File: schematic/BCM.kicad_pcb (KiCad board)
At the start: 4 copper layers, 67 parts, among them P401 POWERCON, P402 KEYSWITCH, P403 CHARGESW, P601 BRUSA_CANCON, P602 A123_CANCON, P603 CON+, P604 CON-, P605 CONPRE, P606 UART, Q1 IRF7101PbF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

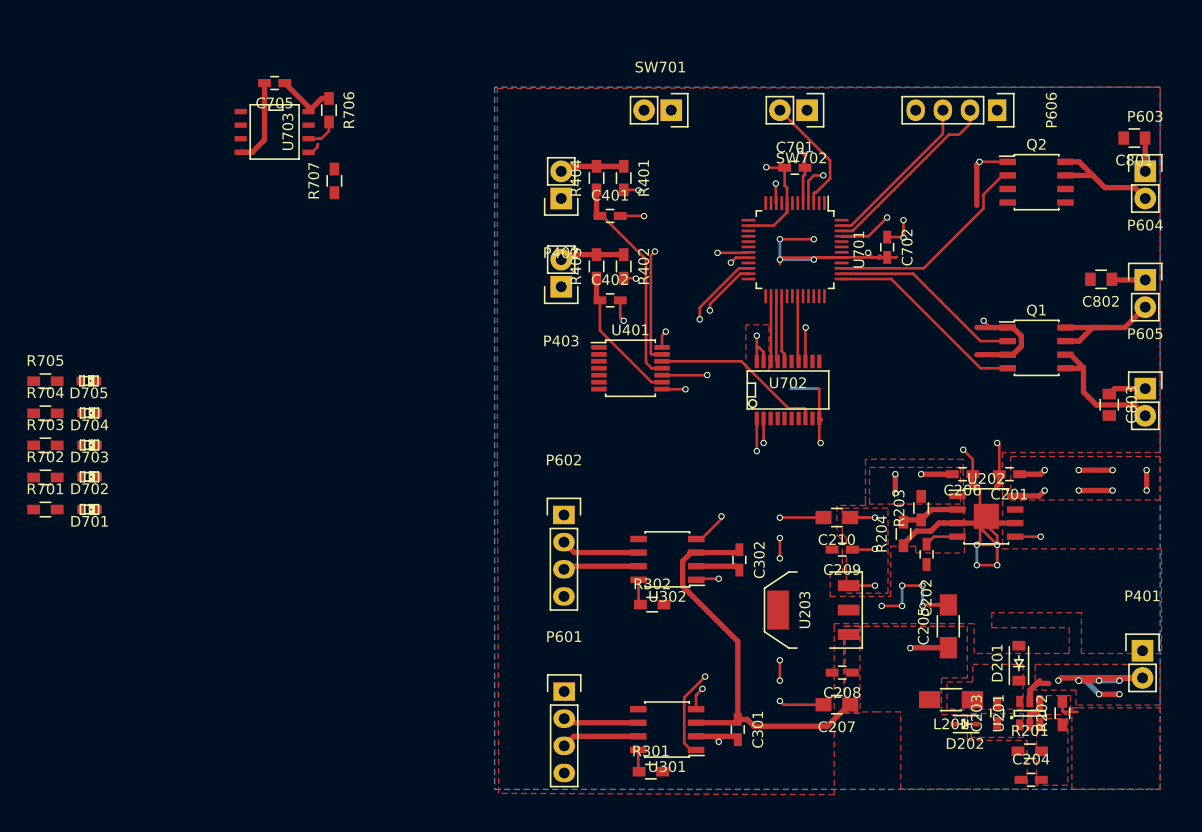
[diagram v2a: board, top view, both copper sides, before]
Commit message: [routing] finished routing passed all DRCs moved pins to accomodate routing
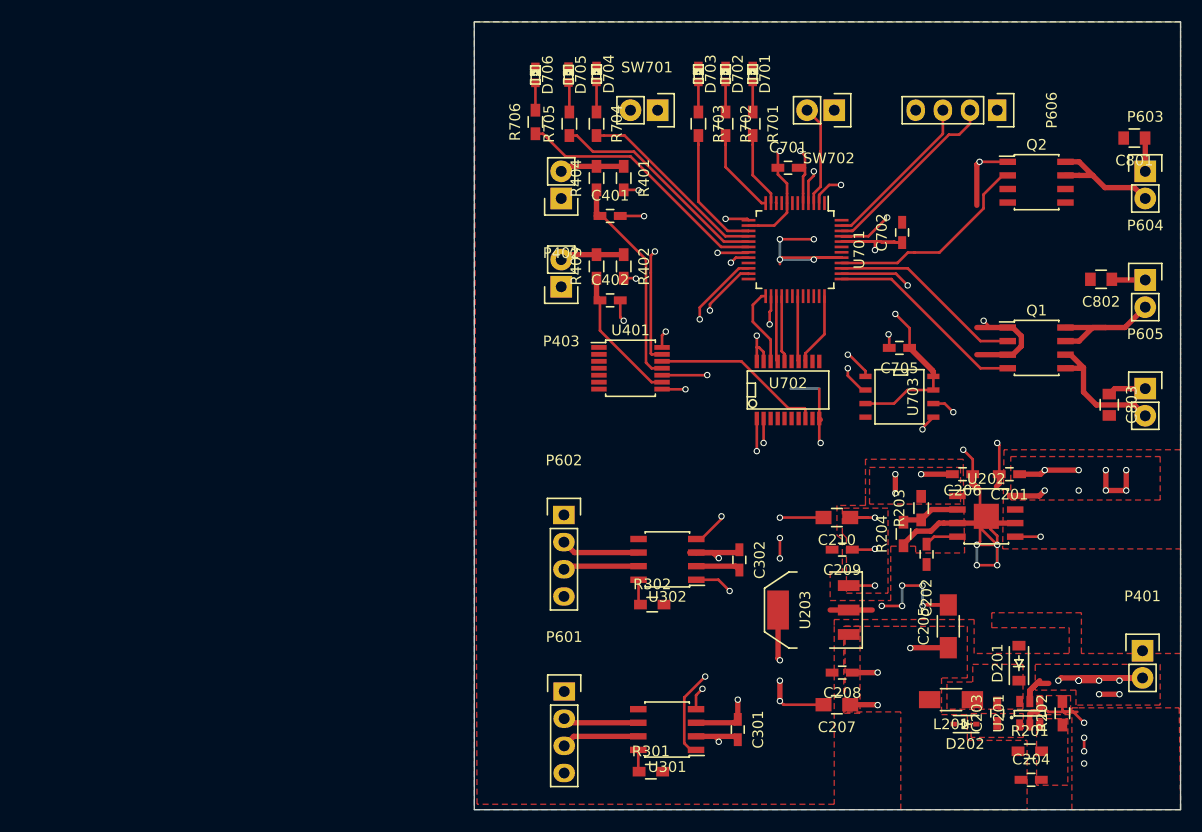
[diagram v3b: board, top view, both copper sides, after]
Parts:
- removed R707: 1k, Resistors_SMD:R_0603_HandSoldering
- added D706: RED, LEDs:LED-0603, F.Cu at (114.3, 121.2)
- R701, R702, R703, R704, R705: value 330 -> 1k
- U703: value 24C16 -> AT25XX
- moved R701 75.3 mm to (134.6, 125.7), turned to 270 degrees
- moved D701 74.2 mm to (134.6, 121.1), turned to 270 degrees
- moved R702 71.7 mm to (132.1, 125.7), turned to 270 degrees
- moved D702 70.4 mm to (132.1, 121.1), turned to 270 degrees
- moved R703 68.1 mm to (129.5, 125.7), turned to 270 degrees
- moved D703 66.7 mm to (129.5, 121.1), turned to 270 degrees
- moved C705 63.5 mm to (148.3, 146.7)
- moved U703 63.5 mm to (148.3, 151.3)
- moved R704 58.2 mm to (120.0, 125.7), turned to 270 degrees
- moved D704 57.0 mm to (120.0, 121.1), turned to 270 degrees
- moved R705 54.6 mm to (117.5, 125.7), turned to 90 degrees
- moved D705 53.2 mm to (117.4, 121.1), turned to 270 degrees
- moved R706 19.3 mm to (114.3, 125.6), turned to 90 degrees
- moved SW702 2.54 mm to (142.2, 124.5)
- moved C702 1.97 mm to (148.6, 135.9), turned to 90 degrees
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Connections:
- C209 pad 1: VCC -> +3V3
- C210 pad 1: VCC -> +3V3
- C701 pad 1: VCC -> +3V3
- C702 pad 1: VCC -> +3V3
- C705 pad 1: VCC -> +3V3
- R401 pad 2: VCC -> +3V3
- R402 pad 2: VCC -> +3V3
- R701 pad 2: /microController/IO_LED03 -> /microController/IO_LED0
- R702 pad 2: /microController/IO_LED02 -> /microController/IO_LED1
- R703 pad 2: Net-(R703-Pad2) -> /microController/IO_LED2
- R704 pad 2: /microController/IO_LED00 -> /microController/IO_LED3
- R705 pad 1: /microController/IO_LED10 -> /microController/IO_LED4
- R706 pad 1: VCC -> /microController/IO_LED5
- R706 pad 2: /microController/EEPROM_SCL -> Net-(D706-Pad2)
- U203 pad 3: VCC -> +3V3
- U401 pad 14: VCC -> +3V3
- U701 pad 10: /microController/CAN1_INT -> Net-(U701-Pad10)
- U701 pad 11: Net-(U701-Pad11) -> /microController/IO_LED0
- U701 pad 12: Net-(U701-Pad12) -> /microController/IO_LED1
- U701 pad 13: Net-(U701-Pad13) -> /microController/PROM_SCK
- U701 pad 14: VCC -> +3V3
- U701 pad 15: /microController/EEPROM_SCL -> /microController/IO_LED2
- U701 pad 16: /microController/EEPROM_SDA -> /microController/IO_LED3
- U701 pad 17: Net-(U701-Pad17) -> /microController/IO_LED4
- U701 pad 18: Net-(U701-Pad18) -> /microController/IO_LED5
- U701 pad 2: Net-(U701-Pad2) -> /microController/PROM_SSEL
- U701 pad 25: /microController/IO_LED10 -> /microController/CAN1_SSEL
- U701 pad 26: /microController/CAN1_SSEL -> /microController/PROM_MISO
- U701 pad 36: /microController/IO_LED00 -> /microController/CAN1_INT
- U701 pad 38: /Contactor Driver/CON- -> /microController/PROM_MOSI
- U701 pad 39: /Contactor Driver/CON+ -> /Contactor Driver/CON-
- U701 pad 40: Net-(U701-Pad40) -> /Contactor Driver/CON+
- U701 pad 43: /microController/IO_LED02 -> Net-(U701-Pad43)
- U701 pad 44: VCC -> +3V3
- U701 pad 48: /microController/IO_LED03 -> Net-(U701-Pad48)
- U701 pad 8: VCC -> +3V3
- U702 pad 19: VCC -> +3V3
- U702 pad 20: VCC -> +3V3
- U703 pad 1: Net-(U703-Pad1) -> /microController/PROM_SSEL
- U703 pad 2: Net-(U703-Pad2) -> /microController/PROM_MISO
- U703 pad 3: Net-(U703-Pad3) -> +3V3
- U703 pad 5: /microController/EEPROM_SDA -> /microController/PROM_MOSI
- U703 pad 6: /microController/EEPROM_SCL -> /microController/PROM_SCK
- U703 pad 7: Net-(U703-Pad7) -> +3V3
- U703 pad 8: VCC -> +3V3
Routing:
- net +3V3: track 0.00 -> 62.0 mm, vias 0 -> 10
- net +5V: track 102.9 -> 47.5 mm, vias 1 -> 5
- net VCC: track 41.0 -> 0.00 mm, vias 10 -> 0
- net /microController/PROM_SCK: track 0.00 -> 38.9 mm, vias 0 -> 2
- net /microController/IO_LED5: track 0.00 -> 24.3 mm
- net /microController/PROM_MOSI: track 0.00 -> 22.2 mm, vias 0 -> 2
- net /microController/PROM_SSEL: track 0.00 -> 22.1 mm, vias 0 -> 2
- net /microController/IO_LED4: track 0.00 -> 20.9 mm
- net /microController/IO_LED3: track 0.00 -> 18.1 mm
- net /microController/PROM_MISO: track 0.00 -> 14.6 mm, vias 0 -> 2
- net /microController/CAN1_INT: track 19.9 -> 6.98 mm, vias 2 -> 0
- net /microController/IO_LED2: track 0.00 -> 12.0 mm
- net /microController/IO_LED1: track 0.00 -> 8.09 mm
- net /microController/IO_LED0: track 0.00 -> 7.02 mm
- net GND: track 148.1 -> 154.0 mm, vias 29 -> 33
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- added copper zone on F.Cu, net +3V3
- added copper zone on In1.Cu, net +3V3
- added copper zone on In1.Cu, net +5V
- removed copper zone on F.Cu, net VCC
- removed copper zone on In1.Cu, net VCC
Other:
- board outline added: 66 x 73.7 mm
- rule trace_min: 0.2 -> 0.007874
- rule via_min_size: 0.4 -> 0.015748

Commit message: Final change before fab
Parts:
- moved C201 78.0 mm to (143.4, 82.0)
- moved C202 78.0 mm to (135.6, 89.5)
- moved C203 78.0 mm to (142.2, 104.4)
- moved C206 78.0 mm to (139.0, 82.0)
- moved C207 78.0 mm to (127.2, 103.6)
- moved C208 78.0 mm to (127.7, 100.6)
- moved C209 78.0 mm to (127.7, 89.1)
- moved C210 78.0 mm to (127.2, 86.1)
- moved C301 78.0 mm to (118.0, 105.9)
- moved C302 78.0 mm to (118.1, 90.1)
- moved C401 78.0 mm to (106.0, 57.9)
- moved C402 78.0 mm to (106.0, 65.8)
- moved C701 78.0 mm to (122.7, 53.4)
- moved C705 78.0 mm to (133.1, 70.2)
- moved C801 78.0 mm to (155.1, 50.6)
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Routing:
- net GND: track 154.0 -> 157.1 mm
- net (no net): track 4.57 -> 2.67 mm, vias 2 -> 0
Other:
- net class Default: via_dia 0.6 -> 0.8
- net class POWER: via_dia 0.6 -> 0.8
